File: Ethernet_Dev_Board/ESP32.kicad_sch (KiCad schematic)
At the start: 22 parts, among them J401 TAG-CONNECT_NL_10-POS_LEGS, U402 ESP32-WROOM-32E, U403 74LVC1G11W6

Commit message: Rev A Design files finish
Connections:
- net GND1: now also J402.13
- net IO21 renamed ETH_RST
- net ETH_RST: no longer J402.13
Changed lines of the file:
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@@
 	)
 	(junction
+		(at 204.47 121.92)
+		(diameter 0)
+		(color 0 0 0 0)
+	)
+	(junction
 		(at 160.02 128.27)
 		(diameter 0)
@@
 	(wire
 		(pts
+			(xy 204.47 119.38) (xy 204.47 121.92)
+		)
+		(stroke
+			(width 0)
+			(type default)
+		)
+	)
+	(wire
+		(pts
 			(xy 204.47 114.3) (xy 207.01 114.3)
 		)
@@
 	(wire
 		(pts
-			(xy 172.72 50.8) (xy 193.04 50.8)
+			(xy 172.72 50.8) (xy 191.77 50.8)
 		)
 		(stroke
@@
 	)
 	(symbol
-		(lib_id "RG_Symbols:INPUT_7")
-		(at 201.93 119.38 180)
-		(unit 1)
-		(exclude_from_sim no)
-		(in_bom yes)
-		(on_board yes)
-		(dnp no)
-		(property "Reference" "#NetPort0444"
-			(at 201.93 119.38 0)
-			(effects
-				(font
-					(size 1.27 1.27)
-				)
-				(hide yes)
-			)
-		)
-		(property "Value" "IO21"
-			(at 196.85 119.38 0)
-			(effects
-				(font
-					(size 1.27 1.27)
-				)
-			)
-		)
-		(property "Footprint" ""
-			(at 201.93 119.38 0)
-			(effects
-				(font
-					(size 1.27 1.27)
-				)
-				(hide yes)
-			)
-		)
-		(property "Datasheet" ""
-			(at 201.93 119.38 0)
-			(effects
-				(font
-					(size 1.27 1.27)
-				)
-				(hide yes)
-			)
-		)
-		(property "Description" ""
-			(at 201.93 119.38 0)
-			(effects
-				(font
-					(size 1.27 1.27)
-				)
-				(hide yes)
-			)
-		)
-		(property "Mfg." ""
-			(at 201.93 119.38 0)
-			(effects
-				(font
-					(size 1.27 1.27)
-				)
-				(hide yes)
-			)
-		)
-		(property "Mfg. PN" ""
-			(at 201.93 119.38 0)
-			(effects
-				(font
-					(size 1.27 1.27)
-				)
-				(hide yes)
-			)
-		)
-		(property "Distributor" ""
-			(at 201.93 119.38 0)
-			(effects
-				(font
-					(size 1.27 1.27)
-				)
-				(hide yes)
-			)
-		)
-		(property "Distributor PN" ""
-			(at 201.93 119.38 0)
-			(effects
-				(font
-					(size 1.27 1.27)
-				)
-				(hide yes)
-			)
-		)
-		(pin "1"
-		)
-		(instances
-			(project "Ethernet_Dev_Board"
-				(path "/79118fbd-6cbf-48b1-af39-9f7b00f17642/7e416bb0-9118-4a80-b9f7-03742cbffb61"
-					(reference "#NetPort0444")
-					(unit 1)
-				)
-			)
-		)
-	)
-	(symbol
 		(lib_id "LED_Controller_Hardware-eagle-import:IO0")
 		(at 164.465 128.27 0)
@@
 	)
 	(symbol
-		(lib_id "RG_Symbols:Netport")
-		(at 195.58 50.8 0)
-		(unit 1)
-		(exclude_from_sim no)
-		(in_bom yes)
-		(on_board yes)
-		(dnp no)
-		(fields_autoplaced yes)
-		(property "Reference" "#NetPort0432"
-			(at 195.58 53.34 0)
-			(effects
-				(font
-					(size 1.27 1.27)
-				)
-				(hide yes)
-			)
-		)
-		(property "Value" "IO21"
-			(at 197.866 50.8 0)
-			(effects
-				(font
-					(size 1.27 1.27)
-				)
-			)
-		)
-		(property "Footprint" ""
-			(at 195.58 50.8 0)
-			(effects
-				(font
-					(size 1.27 1.27)
-				)
-				(hide yes)
-			)
-		)
-		(property "Datasheet" ""
-			(at 195.58 50.8 0)
-			(effects
-				(font
-					(size 1.27 1.27)
-				)
-				(hide yes)
-			)
-		)
-		(property "Description" ""
-			(at 195.58 50.8 0)
-			(effects
-				(font
-					(size 1.27 1.27)
-				)
-				(hide yes)
-			)
-		)
-		(property "Mfg." ""
-			(at 195.58 50.8 0)
-			(effects
-				(font
-					(size 1.27 1.27)
-				)
-				(hide yes)
-			)
-		)
-		(property "Mfg. PN" ""
-			(at 195.58 50.8 0)
-			(effects
-				(font
-					(size 1.27 1.27)
-				)
-				(hide yes)
-			)
-		)
-		(property "Distributor" ""
-			(at 195.58 50.8 0)
-			(effects
-				(font
-					(size 1.27 1.27)
-				)
-				(hide yes)
-			)
-		)
-		(property "Distributor PN" ""
-			(at 195.58 50.8 0)
-			(effects
-				(font
-					(size 1.27 1.27)
-				)
-				(hide yes)
-			)
-		)
-		(pin "1"
-		)
-		(instances
-			(project "Ethernet_Dev_Board"
-				(path "/79118fbd-6cbf-48b1-af39-9f7b00f17642/7e416bb0-9118-4a80-b9f7-03742cbffb61"
-					(reference "#NetPort0432")
-					(unit 1)
-				)
-			)
-		)
-	)
-	(symbol
 		(lib_id "power:GNDS")
 		(at 76.835 186.69 0)
@@
 					(unit 1)
 				)
+			)
+		)
+	)
+	(symbol
+		(lib_id "LED_Controller_Hardware-eagle-import:SCK")
+		(at 194.31 50.8 0)
+		(unit 1)
+		(exclude_from_sim no)
+		(in_bom yes)
+		(on_board yes)
+		(dnp no)
+		(property "Reference" "#NetPort0448"
+			(at 194.31 50.8 0)
+			(effects
+				(font
+					(size 1.27 1.27)
+				)
+				(hide yes)
+			)
+		)
+		(property "Value" "ETH_RST"
+			(at 198.628 50.8 0)
+			(effects
+				(font
+					(size 1.27 1.27)
+				)
+			)
+		)
+		(property "Footprint" ""
+			(at 194.31 50.8 0)
+			(effects
+				(font
+					(size 1.27 1.27)
+				)
+				(hide yes)
+			)
+		)
+		(property "Datasheet" ""
+			(at 194.31 50.8 0)
+			(effects
+				(font
+					(size 1.27 1.27)
+				)
+				(hide yes)
+			)
+		)
+		(property "Description" ""
+			(at 194.31 50.8 0)
+			(effects
+				(font
+					(size 1.27 1.27)
+				)
+				(hide yes)
+			)
+		)
+		(property "Mfg." ""
+			(at 194.31 50.8 0)
+			(effects
+				(font
+					(size 1.27 1.27)
+				)
+				(hide yes)
+			)
+		)
+		(property "Mfg. PN" ""
+			(at 194.31 50.8 0)
+			(effects
+				(font
+					(size 1.27 1.27)
+				)
+				(hide yes)
+			)
+		)
+		(property "Distributor" ""
+			(at 194.31 50.8 0)
+			(effects
+				(font
+					(size 1.27 1.27)
+				)
+				(hide yes)
+			)
+		)
+		(property "Distributor PN" ""
+			(at 194.31 50.8 0)
+			(effects
+				(font
+					(size 1.27 1.27)
+				)
+				(hide yes)
+			)
+		)
+		(pin "1"
+		)
+		(instances
+			(project "Ethernet_Dev_Board"
+				(path "/79118fbd-6cbf-48b1-af39-9f7b00f17642/7e416bb0-9118-4a80-b9f7-03742cbffb61"
+					(reference "#NetPort0448")
+					(unit 1)
+				)

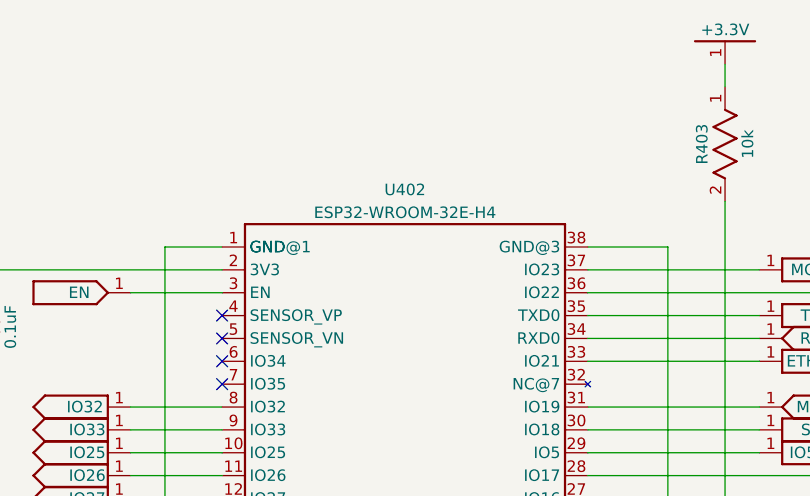
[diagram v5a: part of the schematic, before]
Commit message: Added ordering BOM for REV A
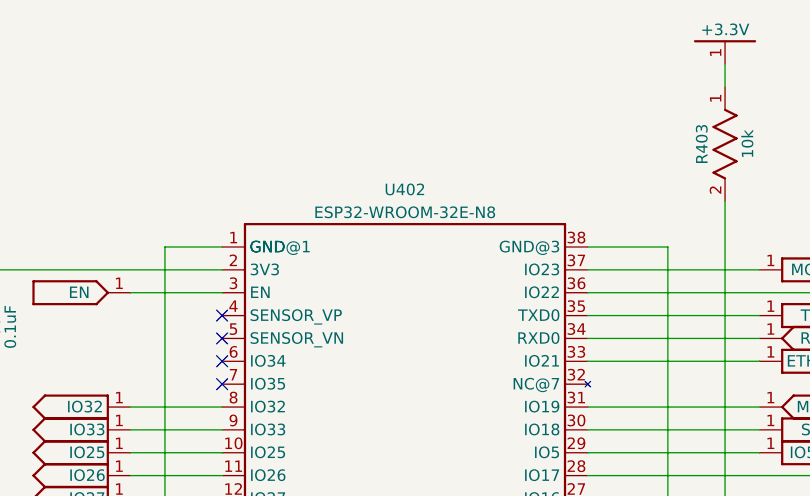
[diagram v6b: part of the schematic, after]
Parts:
- U402: Distributor PN 1965-ESP32-WROOM-32E-H4TR-ND -> 1965-ESP32-WROOM-32E-N8TR-ND; Mfg. PN ESP32-WROOM-32E-H4 -> ESP32-WROOM-32E-N8
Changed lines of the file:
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@@
 			)
 		)
-		(property "Description" "ESP32 w/ PCB Antenna"
+		(property "Description" "RF TXRX MODULE BT PCB TRACE SMD"
 			(at 152.4 55.88 0)
 			(effects
@@
 			)
 		)
-		(property "Mfg. PN" "ESP32-WROOM-32E-H4"
+		(property "Mfg. PN" "ESP32-WROOM-32E-N8"
 			(at 152.4 34.29 0)
 			(effects
@@
 			)
 		)
-		(property "Distributor PN" "1965-ESP32-WROOM-32E-H4TR-ND"
+		(property "Distributor PN" "1965-ESP32-WROOM-32E-N8TR-ND"
 			(at 152.4 55.88 0)
 			(effects
@@
 			)
 		)
-		(property "Description" "6 x 6 mm, 6.5 mm Actuator Height, 260 gf, Black, Surface Mount, SPST, Tactile Switch"
+		(property "Description" "SWITCH TACTILE SPST-NO 0.05A 12V"
 			(at 142.24 128.27 0)
 			(effects
@@
 			)
 		)
-		(property "Description" "CAP-0603"
+		(property "Description" "CAP CER 2.2UF 10V X5R 0603"
 			(at 76.835 176.53 0)
 			(effects
@@
 			)
 		)
-		(property "Description" ""
+		(property "Description" "CAP-0603"
 			(at 91.44 46.99 0)
 			(effects
